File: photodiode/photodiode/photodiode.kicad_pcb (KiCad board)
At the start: 2 copper layers, 18.3 x 14.7 mm, 3 parts, among them J1 Conn_01x03_Male

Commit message: Rev 2 of photodiode PCB
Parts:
- moved R1 7.71 mm to (110.6, 69.9)
- moved D1 6.89 mm to (111.5, 76.7), turned to 180 degrees
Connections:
- D1 pad 1: GND -> VCC
- R1 pad 1: VCC -> GND
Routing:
- net GND: track 9.02 -> 1.10 mm, vias 1 -> 6
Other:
- board text added: "GND"
- board text added: "REV 2 - NOV. 20"
- board text added: "SIG"
- board text added: "VCC"
- board text removed: "Note Diode"
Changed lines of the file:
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@@
-(kicad_pcb (version 20171130) (host pcbnew "(5.1.4)-1")
+(kicad_pcb (version 20171130) (host pcbnew "(5.0.1)-4")
   (general
     (thickness 1.6)
-    (drawings 8)
-    (tracks 11)
+    (drawings 11)
+    (tracks 17)
     (zones 0)
     (modules 3)
@@
   )
   (setup
-    (last_trace_width 0.25)
+    (last_trace_width 0.3048)
+    (user_trace_width 0.3048)
     (trace_clearance 0.2)
     (zone_clearance 0.508)
     (zone_45_only no)
     (trace_min 0.2)
+    (segment_width 0.2)
+    (edge_width 0.05)
     (via_size 0.8)
     (via_drill 0.4)
@@
     (uvia_min_size 0.2)
     (uvia_min_drill 0.1)
-    (edge_width 0.05)
-    (segment_width 0.2)
     (pcb_text_width 0.3)
     (pcb_text_size 1.5 1.5)
@@
     (solder_mask_min_width 0.25)
     (aux_axis_origin 0 0)
-    (visible_elements FFFFFF7F)
+    (visible_elements 7FFFFFFF)
     (pcbplotparams
       (layerselection 0x010fc_ffffffff)
@@
       (drillshape 0)
       (scaleselection 1)
-      (outputdirectory ""))
+      (outputdirectory "REV 2 GERBER/"))
   )
   (net 0 "")
@@
   )
   (module Connector_PinHeader_2.54mm:PinHeader_1x02_P2.54mm_Vertical (layer F.Cu)
-    (at 111.76 69.85)
+    (at 111.52886 76.7334 180)
     (descr "Through hole straight pin header, 1x02, 2.54mm pitch, single row")
     (tags "Through hole pin header THT 1x02 2.54mm single row")
-    (fp_text reference D1 (at -2.54 -0.254) (layer F.SilkS)
-      (effects (font (size 1 1) (thickness 0.15)))
-    )
-    (fp_text value D_Photo (at 0 4.87) (layer F.Fab)
+    (fp_text reference D1 (at -2.54 -0.254 180) (layer F.SilkS)
+      (effects (font (size 1 1) (thickness 0.15)))
+    )
+    (fp_text value D_Photo (at 0 4.87 180) (layer F.Fab)
       (effects (font (size 1 1) (thickness 0.15)))
     )
@@
     (fp_line (start 1.8 4.35) (end 1.8 -1.8) (layer F.CrtYd) (width 0.05))
     (fp_line (start 1.8 -1.8) (end -1.8 -1.8) (layer F.CrtYd) (width 0.05))
-    (fp_text user %R (at 0 1.27 90) (layer F.Fab)
-      (effects (font (size 1 1) (thickness 0.15)))
-    )
-    (pad 1 thru_hole rect (at 0 0) (size 1.7 1.7) (drill 1) (layers *.Cu *.Mask)
-      (net 1 GND))
-    (pad 2 thru_hole oval (at 0 2.54) (size 1.7 1.7) (drill 1) (layers *.Cu *.Mask)
+    (fp_text user %R (at 0 1.27 270) (layer F.Fab)
+      (effects (font (size 1 1) (thickness 0.15)))
+    )
+    (pad 1 thru_hole rect (at 0 0 180) (size 1.7 1.7) (drill 1) (layers *.Cu *.Mask)
+      (net 3 VCC))
+    (pad 2 thru_hole oval (at 0 2.54 180) (size 1.7 1.7) (drill 1) (layers *.Cu *.Mask)
       (net 2 /A0))
     (model ${KISYS3DMOD}/Connector_PinHeader_2.54mm.3dshapes/PinHeader_1x02_P2.54mm_Vertical.wrl
@@
   )
   (module Resistor_SMD:R_0805_2012Metric (layer F.Cu)
-    (at 111.76 77.47)
+    (at 110.58144 69.85508)
     (descr "Resistor SMD 0805 (2012 Metric), square (rectangular) end terminal, IPC_7351 nominal, (Body size source: https://docs.google.com/spreadsheets/d/1BsfQQcO9C6DZCsRaXUlFlo91Tg2WpOkGARC1WS5S8t0/edit?usp=sharing), generated with kicad-footprint-generator")
     (tags resistor)
@@
     )
     (pad 1 smd roundrect (at -0.9375 0) (size 0.975 1.4) (layers F.Cu F.Paste F.Mask) (roundrect_rratio 0.25)
-      (net 3 VCC))
+      (net 1 GND))
     (pad 2 smd roundrect (at 0.9375 0) (size 0.975 1.4) (layers F.Cu F.Paste F.Mask) (roundrect_rratio 0.25)
       (net 2 /A0))
@@
       (rotate (xyz 0 0 0))
     )
+  )
+  (gr_text "REV 2 - NOV. 20" (at 107.74934 67.2211) (layer F.SilkS)
+    (effects (font (size 0.75 0.75) (thickness 0.1875)))
+  )
+  (gr_text "VCC\n" (at 100.711 76.86548) (layer F.SilkS)
+    (effects (font (size 1 1) (thickness 0.25)))
+  )
+  (gr_text SIG (at 100.76942 74.2061) (layer F.SilkS)
+    (effects (font (size 1 1) (thickness 0.25)))
+  )
+  (gr_text GND (at 100.59416 71.63054) (layer F.SilkS)
+    (effects (font (size 1 1) (thickness 0.25)))
   )
   (gr_line (start 100.584 68.556) (end 100.584 68.58) (layer F.SilkS) (width 0.12))
@@
   (gr_circle (center 114.808 67.056) (end 116.308 67.056) (layer Edge.Cuts) (width 0.12))
   (gr_circle (center 100.584 67.056) (end 102.084 67.056) (layer Edge.Cuts) (width 0.12))
-  (gr_text "Note Diode" (at 100.33 74.168 90) (layer F.SilkS)
-    (effects (font (size 1 1) (thickness 0.1)))
-  )
-  (via (at 109.22 74.93) (size 0.8) (drill 0.4) (layers F.Cu B.Cu) (net 1))
   (segment (start 104.14 70.575001) (end 104.14 71.675001) (width 0.25) (layer F.Cu) (net 1))
-  (segment (start 104.865001 69.85) (end 104.14 70.575001) (width 0.25) (layer F.Cu) (net 1))
-  (segment (start 111.76 69.85) (end 104.865001 69.85) (width 0.25) (layer F.Cu) (net 1))
-  (segment (start 112.6975 73.3275) (end 111.76 72.39) (width 0.25) (layer F.Cu) (net 2))
-  (segment (start 112.6975 77.47) (end 112.6975 73.3275) (width 0.25) (layer F.Cu) (net 2))
-  (segment (start 107.394999 74.215001) (end 104.14 74.215001) (width 0.25) (layer F.Cu) (net 2))
-  (segment (start 111.76 72.39) (end 109.22 72.39) (width 0.25) (layer F.Cu) (net 2))
-  (segment (start 109.22 72.39) (end 107.394999 74.215001) (width 0.25) (layer F.Cu) (net 2))
-  (segment (start 110.107501 76.755001) (end 110.8225 77.47) (width 0.25) (layer F.Cu) (net 3))
-  (segment (start 104.14 76.755001) (end 110.107501 76.755001) (width 0.25) (layer F.Cu) (net 3))
+  (via (at 107.86618 75.31608) (size 0.8) (drill 0.4) (layers F.Cu B.Cu) (net 1))
+  (via (at 106.57332 77.86116) (size 0.8) (drill 0.4) (layers F.Cu B.Cu) (net 1))
+  (via (at 109.19714 77.9526) (size 0.8) (drill 0.4) (layers F.Cu B.Cu) (net 1))
+  (via (at 106.73842 73.35012) (size 0.8) (drill 0.4) (layers F.Cu B.Cu) (net 1))
+  (via (at 109.0041 73.40092) (size 0.8) (drill 0.4) (layers F.Cu B.Cu) (net 1))
+  (via (at 107.95508 71.12254) (size 0.8) (drill 0.4) (layers F.Cu B.Cu) (net 1))
+  (segment (start 112.075177 70.411317) (end 111.51894 69.85508) (width 0.3048) (layer F.Cu) (net 2))
+  (segment (start 112.378859 70.714999) (end 112.075177 70.411317) (width 0.3048) (layer F.Cu) (net 2))
+  (segment (start 112.378859 73.343401) (end 112.378859 70.714999) (width 0.3048) (layer F.Cu) (net 2))
+  (segment (start 111.52886 74.1934) (end 112.378859 73.343401) (width 0.3048) (layer F.Cu) (net 2))
+  (segment (start 104.161601 74.1934) (end 104.14 74.215001) (width 0.3048) (layer F.Cu) (net 2))
+  (segment (start 104.14 74.215001) (end 106.081841 72.27316) (width 0.3048) (layer F.Cu) (net 2))
+  (segment (start 109.60862 72.27316) (end 111.52886 74.1934) (width 0.3048) (layer F.Cu) (net 2))
+  (segment (start 106.081841 72.27316) (end 109.60862 72.27316) (width 0.3048) (layer F.Cu) (net 2))
+  (segment (start 111.507259 76.755001) (end 111.52886 76.7334) (width 0.3048) (layer F.Cu) (net 3))
+  (segment (start 104.14 76.755001) (end 111.507259 76.755001) (width 0.3048) (layer F.Cu) (net 3))
   (zone (net 1) (net_name GND) (layer F.Cu) (hatch edge 0.508)
     (connect_pads (clearance 0.508))

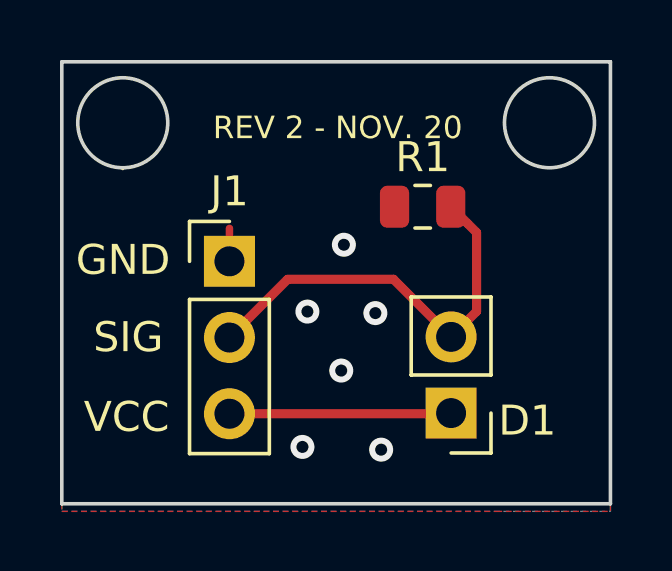
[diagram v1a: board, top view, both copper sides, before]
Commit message: Add voltage divider to photodiode circuit/pcb
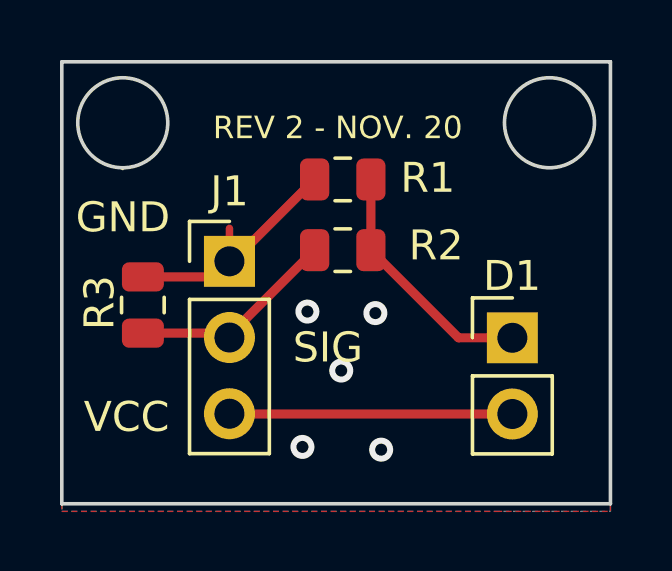
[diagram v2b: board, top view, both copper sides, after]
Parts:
- added R2: R, Resistor_SMD:R_0805_2012Metric, F.Cu at (107.9, 71.3)
- added R3: R, Resistor_SMD:R_0805_2012Metric, F.Cu at (101.3, 73.1)
- moved D1 3.24 mm to (113.6, 74.2), turned to 0 degrees
- moved R1 2.82 mm to (107.9, 68.9)
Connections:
- D1 pad 1: VCC -> Net-(D1-Pad1)
- D1 pad 2: /A0 -> VCC
- R1 pad 2: /A0 -> Net-(D1-Pad1)
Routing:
- net Net-(D1-Pad1): track 0.00 -> 8.28 mm
- net GND: track 1.10 -> 8.17 mm, vias 6 -> 5
- net /A0: track 14.1 -> 7.06 mm
- net VCC: track 7.40 -> 9.43 mm
